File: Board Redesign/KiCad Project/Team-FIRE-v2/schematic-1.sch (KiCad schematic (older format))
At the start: 32 parts

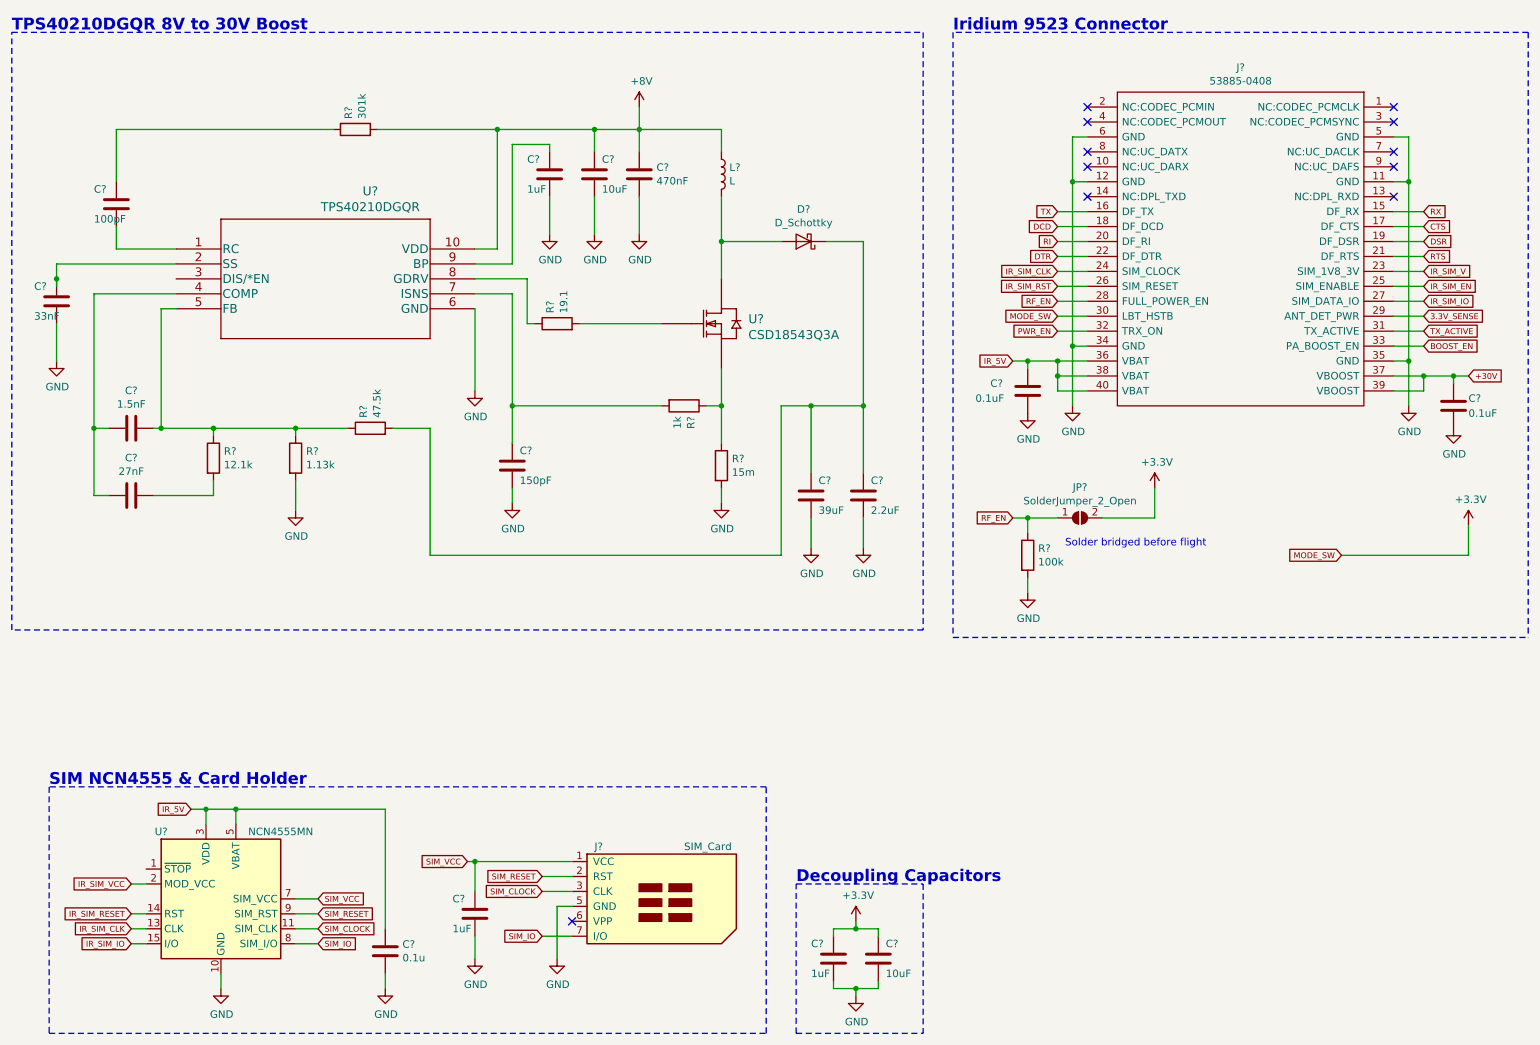
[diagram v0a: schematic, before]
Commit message: Added PMIC part, 3.3V lin reg part, and buck converter + testpoint part
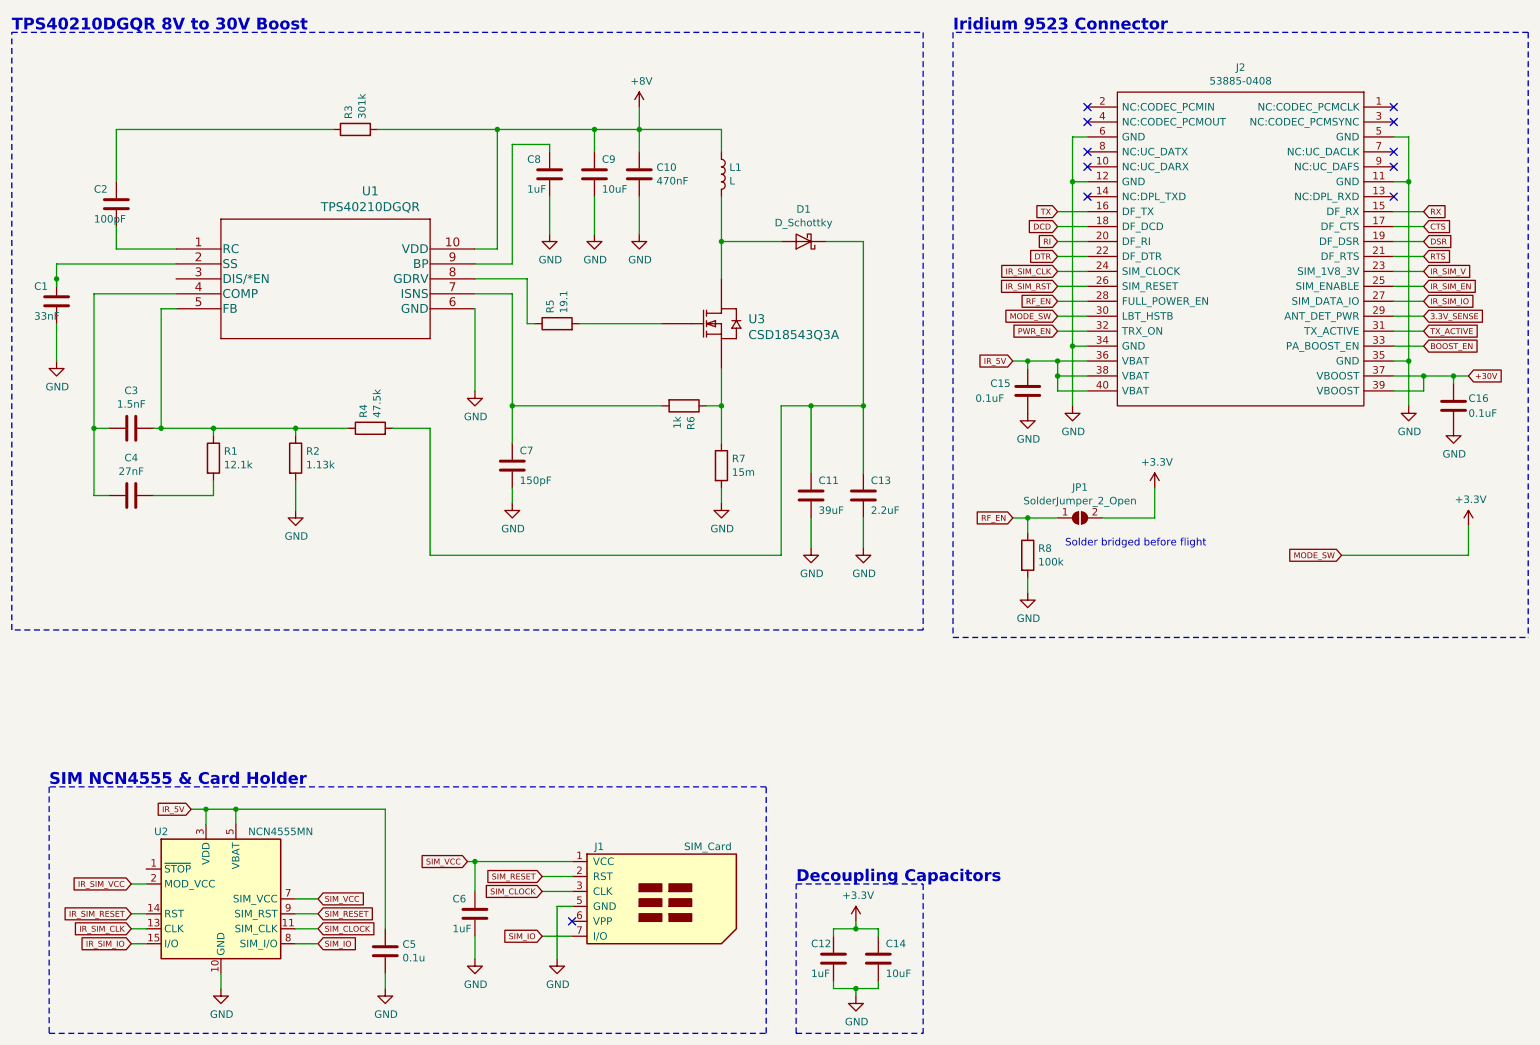
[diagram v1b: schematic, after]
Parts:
- gave numbers to parts that had none: 32

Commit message: Finished PMICs
- Finished stuff on schematic page 3!
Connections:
- net IR_5V renamed +5V
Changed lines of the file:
@@
 	7750 3000 7750 3100
 Connection ~ 7750 3100
-Text GLabel 7450 3000 0    39   Input ~ 0
-IR_5V
 $Comp
 L Device:C C15
@@
 Wire Wire Line
 	2050 6000 2250 6000
-Text GLabel 1950 6000 0    39   Input ~ 0
-IR_5V
 Connection ~ 2050 6000
 Wire Wire Line
@@
 Wire Notes Line
 	6850 800  6850 4800
+$Comp
+L power:+5V #PWR?
+U 1 1 5EA85382
+P 7450 3000
+F 0 "#PWR?" H 7450 2850 50  0001 C CNN
+F 1 "+5V" V 7465 3128 50  0000 L CNN
+F 2 "" H 7450 3000 50  0001 C CNN
+F 3 "" H 7450 3000 50  0001 C CNN
+	1    7450 3000
+	0    -1   -1   0
+$EndComp
+$Comp
+L power:+5V #PWR?
+U 1 1 5EA858F2
+P 1950 6000
+F 0 "#PWR?" H 1950 5850 50  0001 C CNN
+F 1 "+5V" V 1965 6128 50  0000 L CNN
+F 2 "" H 1950 6000 50  0001 C CNN
+F 3 "" H 1950 6000 50  0001 C CNN
+	1    1950 6000
+	0    -1   -1   0
+$EndComp
 $EndSCHEMATC
